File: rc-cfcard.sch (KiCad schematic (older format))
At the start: 13 parts, among them J1 RC2014, J2 RC2014_Enh, J3 CF Socket, U1 74AHCT138, U2 74HCT32, U3 74HC245

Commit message: Fix footprint reference
Fix footprint reference, clean up groundplane routing a little
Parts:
- J3: footprint PD_Parts:CF_Card_Socket -> rc-cfcard:CF_Card_Socket
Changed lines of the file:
@@
 F 0 "J3" H 8600 2015 50  0000 C CNN
 F 1 "CF Socket" H 8600 1924 50  0000 C CNN
-F 2 "PD_Parts:CF_Card_Socket" H 8950 1900 50  0001 L CNN
+F 2 "rc-cfcard:CF_Card_Socket" H 8950 1900 50  0001 L CNN
 F 3 "http://multimedia.3m.com/mws/media/223587O/3mtm-cf-card-hdr-compactflashtm-type-ii-surfacemount-ts2082.pdf" H 8950 1800 50  0001 L CNN
 	1    8100 1750

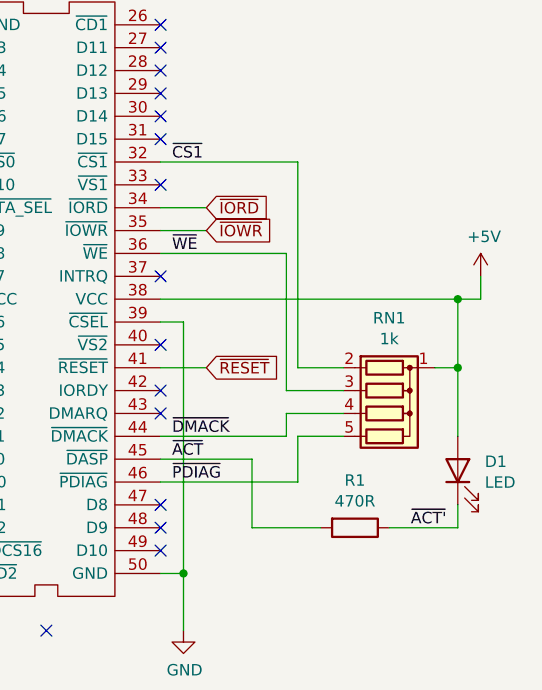
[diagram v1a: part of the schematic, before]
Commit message: Replace resistor network with SMT parts
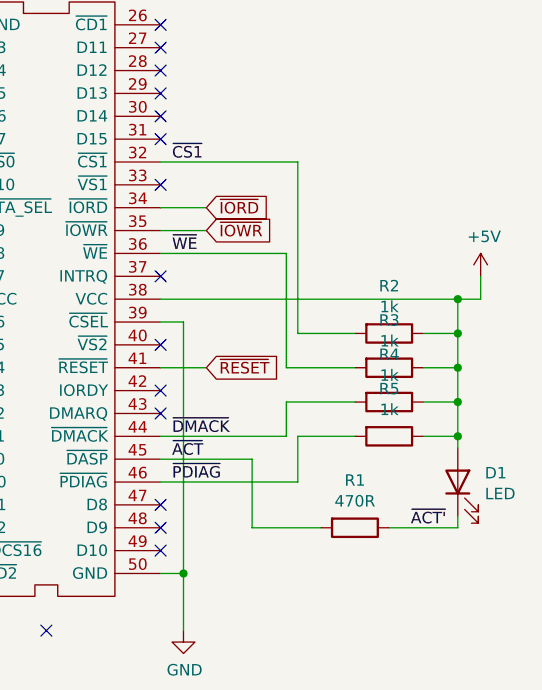
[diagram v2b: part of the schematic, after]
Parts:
- removed RN1: 1k, Resistor_THT:R_Array_SIP5, symbol Device:R_Network04
- added R2, R3, R4, R5: 1k, Resistor_SMD:R_0805_2012Metric, symbol Device:R
- C4: footprint Capacitor_THT:C_Disc_D3.8mm_W2.6mm_P2.50mm -> Capacitor_SMD:C_0805_2012Metric
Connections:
- net +5V: now also R2.1, R3.1, R4.1, R5.1
- net ~CS1: now also R2.2
- net ~DMACK: now also R4.2
- net ~PDIAG: now also R5.2
- net ~WE: now also R3.2
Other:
- moved on the sheet: D1
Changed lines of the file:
@@
 Wire Wire Line
 	8000 2550 8000 2650
-$Comp
-L Device:R_Network04 RN1
-U 1 1 5FC735EF
-P 10100 3450
-F 0 "RN1" V 9683 3450 50  0000 C CNN
-F 1 "1k" V 9774 3450 50  0000 C CNN
-F 2 "Resistor_THT:R_Array_SIP5" V 10375 3450 50  0001 C CNN
-F 3 "http://www.vishay.com/docs/31509/csc.pdf" H 10100 3450 50  0001 C CNN
-	1    10100 3450
-	0    1    1    0
-$EndComp
 Wire Wire Line
 	9100 3750 9700 3750
@@
 	9700 3750 9700 3550
 Wire Wire Line
-	9700 3550 9900 3550
+	9700 3550 9950 3550
 Wire Wire Line
 	9100 2350 9700 2350
 Wire Wire Line
-	9700 2350 9700 3250
-Wire Wire Line
-	9700 3250 9900 3250
-Wire Wire Line
-	9900 3350 9650 3350
-Wire Wire Line
-	9650 3350 9650 2750
+	9700 2350 9700 3100
+Wire Wire Line
+	9700 3100 9950 3100
+Wire Wire Line
+	9950 3250 9650 3250
+Wire Wire Line
+	9650 3250 9650 2750
 Wire Wire Line
 	9650 2750 9100 2750
@@
 	9100 3550 9650 3550
 Wire Wire Line
-	9650 3550 9650 3450
-Wire Wire Line
-	9650 3450 9900 3450
+	9650 3550 9650 3400
+Wire Wire Line
+	9650 3400 9950 3400
 Wire Wire Line
 	9100 2950 10400 2950
@@
 	1    0    0    -1
 $EndComp
-Wire Wire Line
-	10300 3250 10400 3250
-Wire Wire Line
-	10400 3250 10400 2950
 Connection ~ 10400 2950
 Wire Wire Line
@@
 L Device:LED D1
 U 1 1 5FD47530
-P 10400 3700
-F 0 "D1" V 10439 3582 50  0000 R CNN
-F 1 "LED" V 10348 3582 50  0000 R CNN
-F 2 "LED_THT:LED_D3.0mm" H 10400 3700 50  0001 C CNN
-F 3 "~" H 10400 3700 50  0001 C CNN
-	1    10400 3700
+P 10400 3750
+F 0 "D1" V 10439 3632 50  0000 R CNN
+F 1 "LED" V 10348 3632 50  0000 R CNN
+F 2 "LED_THT:LED_D3.0mm" H 10400 3750 50  0001 C CNN
+F 3 "~" H 10400 3750 50  0001 C CNN
+	1    10400 3750
 	0    -1   -1   0
 $EndComp
@@
 	10100 3950 10400 3950
 Wire Wire Line
-	10400 3950 10400 3850
-Wire Wire Line
-	10400 3550 10400 3250
-Connection ~ 10400 3250
+	10400 3950 10400 3900
 Text Label 9150 3650 0    50   ~ 0
 ~ACT
@@
 $EndComp
 $Comp
-L power:+5V #PWR?
+L power:+5V #PWR01
 U 1 1 60023897
 P 2650 1850
-F 0 "#PWR?" H 2650 1700 50  0001 C CNN
+F 0 "#PWR01" H 2650 1700 50  0001 C CNN
 F 1 "+5V" H 2665 2023 50  0000 C CNN
 F 2 "" H 2650 1850 50  0001 C CNN
@@
 	2650 1850 2650 1950
 $Comp
-L power:GND #PWR?
+L power:GND #PWR02
 U 1 1 6002AADF
 P 2650 2350
-F 0 "#PWR?" H 2650 2100 50  0001 C CNN
+F 0 "#PWR02" H 2650 2100 50  0001 C CNN
 F 1 "GND" H 2655 2177 50  0000 C CNN
 F 2 "" H 2650 2350 50  0001 C CNN
@@
 $EndComp
 $Comp
-L power:+5V #PWR?
+L power:+5V #PWR03
 U 1 1 6003AF84
 P 2650 4100
-F 0 "#PWR?" H 2650 3950 50  0001 C CNN
+F 0 "#PWR03" H 2650 3950 50  0001 C CNN
 F 1 "+5V" H 2665 4273 50  0000 C CNN
 F 2 "" H 2650 4100 50  0001 C CNN
@@
 	2650 4100 2650 4200
 $Comp
-L power:GND #PWR?
+L power:GND #PWR04
 U 1 1 6003AF8B
 P 2650 4600
-F 0 "#PWR?" H 2650 4350 50  0001 C CNN
+F 0 "#PWR04" H 2650 4350 50  0001 C CNN
 F 1 "GND" H 2655 4427 50  0000 C CNN
 F 2 "" H 2650 4600 50  0001 C CNN
@@
 F 0 "C4" H 7715 3196 50  0000 L CNN
 F 1 "10uF" H 7715 3105 50  0000 L CNN
-F 2 "Capacitor_THT:C_Disc_D3.8mm_W2.6mm_P2.50mm" H 7638 3000 50  0001 C CNN
+F 2 "Capacitor_SMD:C_0805_2012Metric" H 7638 3000 50  0001 C CNN
 F 3 "~" H 7600 3150 50  0001 C CNN
 	1    7600 3150
@@
 Wire Wire Line
 	7600 2950 7600 3000
+Wire Wire Line
+	10250 3100 10400 3100
+Connection ~ 10400 3100
+Wire Wire Line
+	10400 3100 10400 2950
+Wire Wire Line
+	10400 3600 10400 3550
+$Comp
+L Device:R R2
+U 1 1 5FE6E9D5
+P 10100 3100
+F 0 "R2" V 9893 3100 50  0000 C CNN
+F 1 "1k" V 9984 3100 50  0000 C CNN
+F 2 "Resistor_SMD:R_0805_2012Metric" V 10030 3100 50  0001 C CNN
+F 3 "~" H 10100 3100 50  0001 C CNN
+	1    10100 3100
+	0    1    1    0
+$EndComp
+$Comp
+L Device:R R3
+U 1 1 5FE6EE28
+P 10100 3250
+F 0 "R3" V 9893 3250 50  0000 C CNN
+F 1 "1k" V 9984 3250 50  0000 C CNN
+F 2 "Resistor_SMD:R_0805_2012Metric" V 10030 3250 50  0001 C CNN
+F 3 "~" H 10100 3250 50  0001 C CNN
+	1    10100 3250
+	0    1    1    0
+$EndComp
+$Comp
+L Device:R R4
+U 1 1 5FE6F53D
+P 10100 3400
+F 0 "R4" V 9893 3400 50  0000 C CNN
+F 1 "1k" V 9984 3400 50  0000 C CNN
+F 2 "Resistor_SMD:R_0805_2012Metric" V 10030 3400 50  0001 C CNN
+F 3 "~" H 10100 3400 50  0001 C CNN
+	1    10100 3400
+	0    1    1    0
+$EndComp
+$Comp
+L Device:R R5
+U 1 1 5FE6FC62
+P 10100 3550
+F 0 "R5" V 9893 3550 50  0000 C CNN
+F 1 "1k" V 9984 3550 50  0000 C CNN
+F 2 "Resistor_SMD:R_0805_2012Metric" V 10030 3550 50  0001 C CNN
+F 3 "~" H 10100 3550 50  0001 C CNN
+	1    10100 3550
+	0    1    1    0
+$EndComp
+Wire Wire Line
+	10250 3250 10400 3250
+Connection ~ 10400 3250
+Wire Wire Line
+	10400 3250 10400 3100
+Wire Wire Line
+	10250 3400 10400 3400
+Connection ~ 10400 3400
+Wire Wire Line
+	10400 3400 10400 3250
+Wire Wire Line
+	10250 3550 10400 3550
+Connection ~ 10400 3550
+Wire Wire Line
+	10400 3550 10400 3400
 $EndSCHEMATC

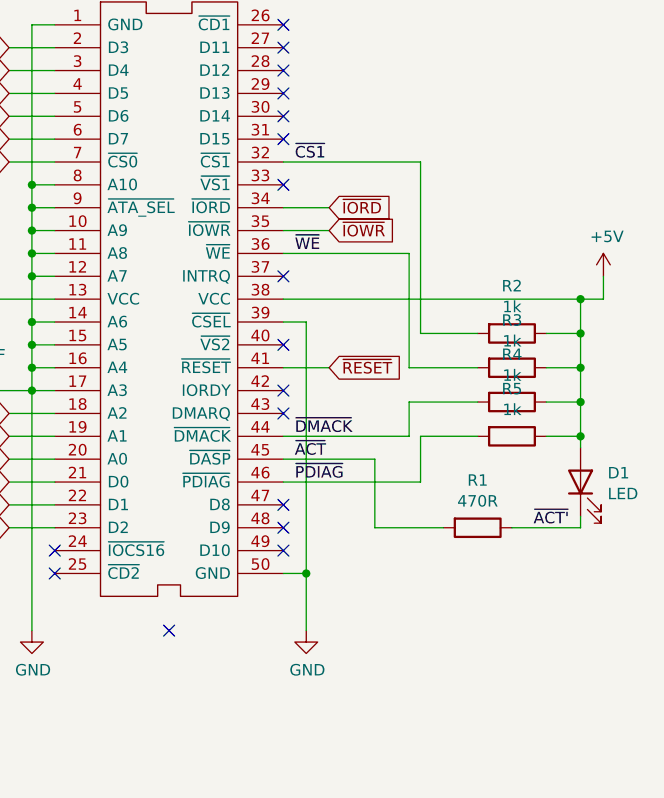
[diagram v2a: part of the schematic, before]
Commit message: Change to through-hole CF socket
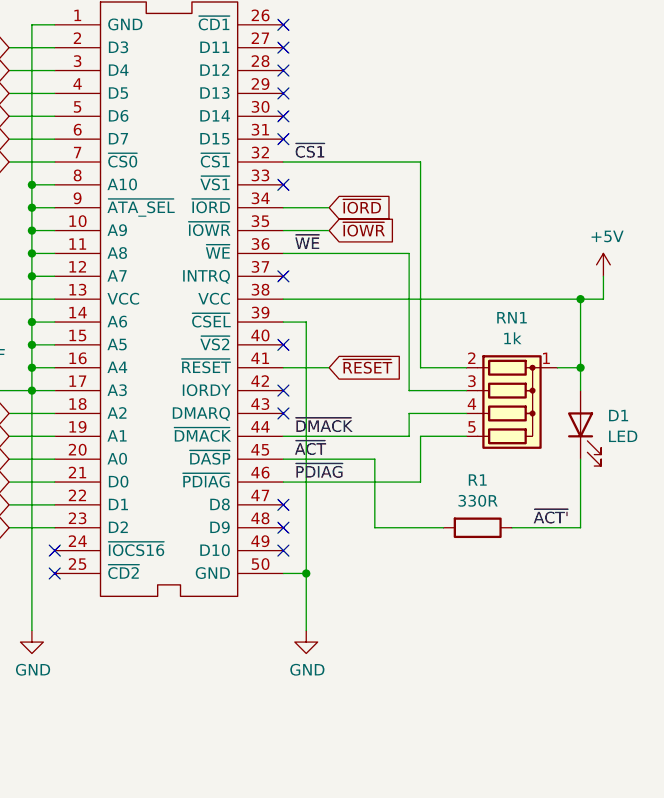
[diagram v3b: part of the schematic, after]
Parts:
- removed R2, R3, R4, R5: 1k, Resistor_SMD:R_0805_2012Metric, symbol Device:R
- added RN1: 1k, Resistor_THT:R_Array_SIP5, symbol Device:R_Network04
- C4: footprint Capacitor_SMD:C_0805_2012Metric -> Capacitor_THT:C_Disc_D3.8mm_W2.6mm_P2.50mm
- J3: footprint rc-cfcard:CF_Card_Socket -> rc-cfcard:CF_Card_Socket_PTH
- R1: value 470R -> 330R
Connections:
- net +5V: now also RN1.1 (common)
- net ~CS1: now also RN1.2 (R1)
- net ~DMACK: now also RN1.4 (R3)
- net ~PDIAG: now also RN1.5 (R4)
- net ~WE: now also RN1.3 (R2)
- no-connect marks 49 -> 48
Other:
- moved on the sheet: D1

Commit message: Re-arranged support chips
Moved buffer and OR gate so that data traces can be more uniform in length
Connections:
- net GND: now also U2.4, U2.5; no longer U2.1, U2.2
- net ~CFCS: now also U2.2; no longer U2.5
- net ~IOCS: now also U2.3, U2.9; no longer U2.10, U2.6
- net ~IORD: now also U2.8; no longer U2.11
- net ~IOREQ: now also U2.1; no longer U2.4
- net ~IOWR: now also U2.11; no longer U2.8
- net ~RD: now also U2.10; no longer U2.13
- net ~WR: now also U2.13; no longer U2.9
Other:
- moved on the sheet: U2A, U2B, U2C, U2D
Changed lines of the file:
@@
 L 74xx:74LS32 U2
 U 2 1 5FCEEE8C
-P 5250 1850
-F 0 "U2" H 5250 2175 50  0000 C CNN
-F 1 "74HCT32" H 5250 2084 50  0000 C CNN
-F 2 "Package_DIP:DIP-14_W7.62mm_LongPads" H 5250 1850 50  0001 C CNN
-F 3 "http://www.ti.com/lit/gpn/sn74LS32" H 5250 1850 50  0001 C CNN
-	2    5250 1850
+P 6100 4150
+F 0 "U2" H 6100 4475 50  0000 C CNN
+F 1 "74HCT32" H 6100 4384 50  0000 C CNN
+F 2 "Package_DIP:DIP-14_W7.62mm_LongPads" H 6100 4150 50  0001 C CNN
+F 3 "http://www.ti.com/lit/gpn/sn74LS32" H 6100 4150 50  0001 C CNN
+	2    6100 4150
 	1    0    0    -1
 $EndComp
@@
 L 74xx:74LS32 U2
 U 1 1 5FCEB7CF
-P 6100 4150
-F 0 "U2" H 6100 4475 50  0000 C CNN
-F 1 "74HCT32" H 6100 4384 50  0000 C CNN
-F 2 "Package_DIP:DIP-14_W7.62mm_LongPads" H 6100 4150 50  0001 C CNN
-F 3 "http://www.ti.com/lit/gpn/sn74LS32" H 6100 4150 50  0001 C CNN
-	1    6100 4150
+P 5250 1850
+F 0 "U2" H 5250 2175 50  0000 C CNN
+F 1 "74HCT32" H 5250 2084 50  0000 C CNN
+F 2 "Package_DIP:DIP-14_W7.62mm_LongPads" H 5250 1850 50  0001 C CNN
+F 3 "http://www.ti.com/lit/gpn/sn74LS32" H 5250 1850 50  0001 C CNN
+	1    5250 1850
 	1    0    0    -1
 $EndComp
@@
 L 74xx:74LS32 U2
 U 3 1 5FCF0690
+P 6250 1550
+F 0 "U2" H 6250 1875 50  0000 C CNN
+F 1 "74HCT32" H 6250 1784 50  0000 C CNN
+F 2 "Package_DIP:DIP-14_W7.62mm_LongPads" H 6250 1550 50  0001 C CNN
+F 3 "http://www.ti.com/lit/gpn/sn74LS32" H 6250 1550 50  0001 C CNN
+	3    6250 1550
+	1    0    0    1
+$EndComp
+Wire Wire Line
+	5850 1650 5950 1650
+Wire Wire Line
+	5750 1450 5950 1450
+$Comp
+L 74xx:74LS32 U2
+U 4 1 5FCF14F5
 P 6250 2150
 F 0 "U2" H 6250 2475 50  0000 C CNN
@@
 F 2 "Package_DIP:DIP-14_W7.62mm_LongPads" H 6250 2150 50  0001 C CNN
 F 3 "http://www.ti.com/lit/gpn/sn74LS32" H 6250 2150 50  0001 C CNN
-	3    6250 2150
-	1    0    0    1
-$EndComp
-Wire Wire Line
-	5850 1650 5950 1650
-Wire Wire Line
-	5750 1450 5950 1450
-$Comp
-L 74xx:74LS32 U2
-U 4 1 5FCF14F5
-P 6250 1550
-F 0 "U2" H 6250 1875 50  0000 C CNN
-F 1 "74HCT32" H 6250 1784 50  0000 C CNN
-F 2 "Package_DIP:DIP-14_W7.62mm_LongPads" H 6250 1550 50  0001 C CNN
-F 3 "http://www.ti.com/lit/gpn/sn74LS32" H 6250 1550 50  0001 C CNN
-	4    6250 1550
-	1    0    0    1
+	4    6250 2150
+	1    0    0    -1
 $EndComp
 $EndSCHEMATC
